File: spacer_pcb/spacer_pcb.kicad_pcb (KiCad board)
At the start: 2 copper layers, 10 x 39.3 mm, 3 parts, among them J1 Conn_01x15, J2 Conn_02x15_Odd_Even, J3 Conn_01x15

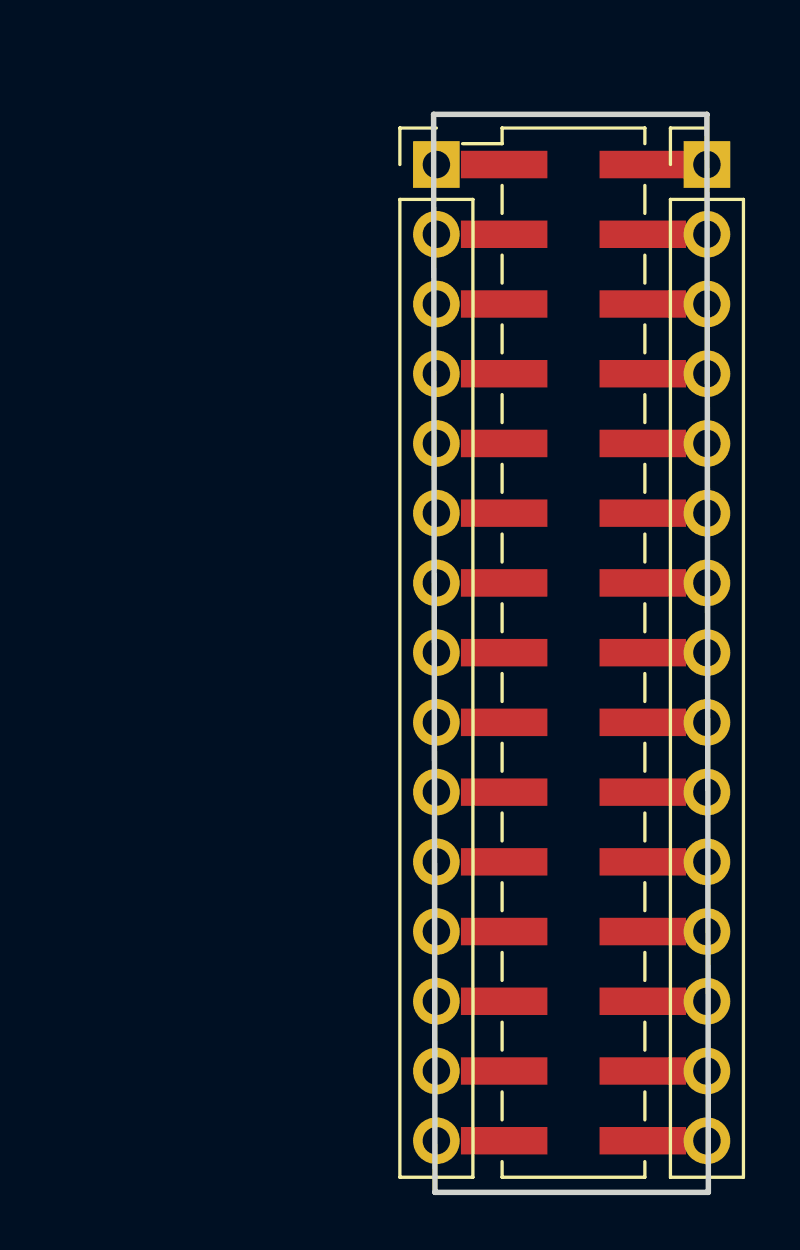
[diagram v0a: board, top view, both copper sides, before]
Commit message: Update connecting hole position between pcb and spacer pcb
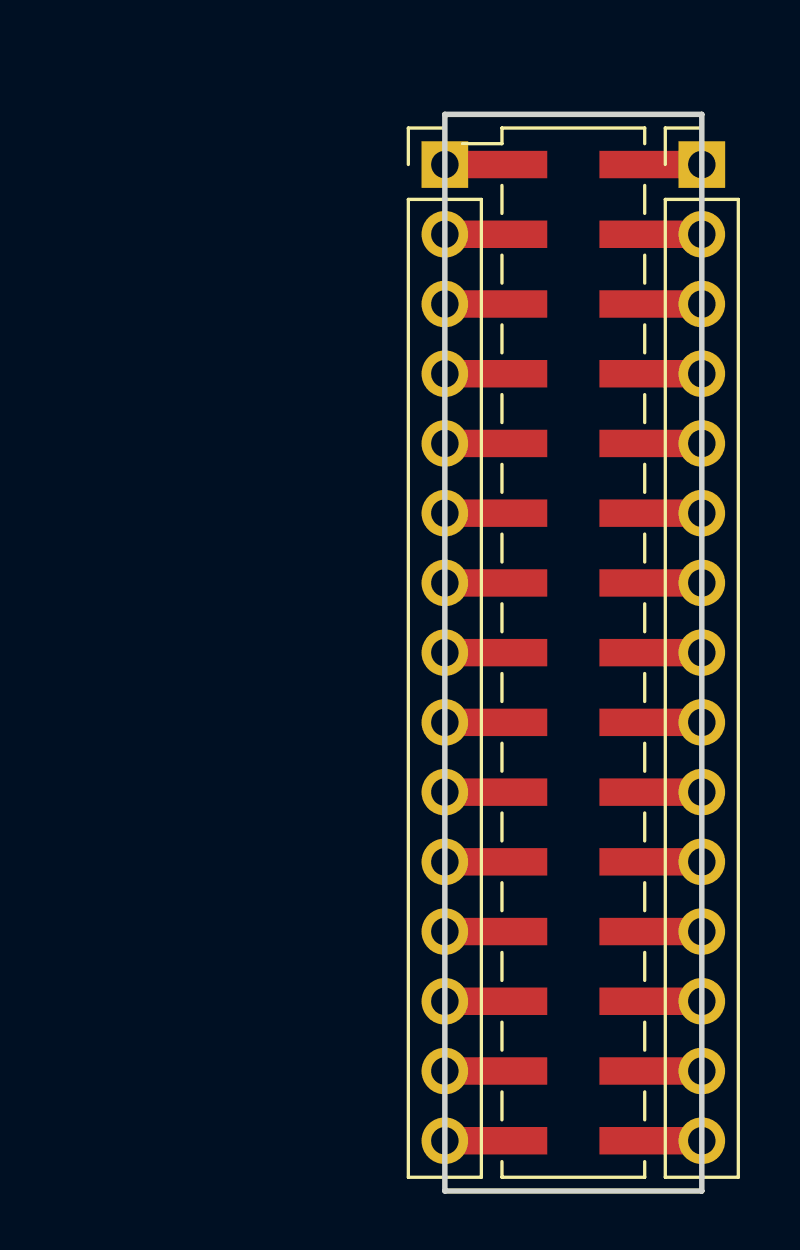
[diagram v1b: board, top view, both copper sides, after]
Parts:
- moved J1 0.31 mm to (131.2, 63.6)
- moved J3 0.19 mm to (140.6, 63.6)
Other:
- board size 10 x 39.3 mm -> 9.4 x 39.2 mm
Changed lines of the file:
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@@
   )
   (module Connector_PinHeader_2.54mm:PinHeader_1x15_P2.54mm_Vertical (layer F.Cu)
-    (at 130.9116 63.5508)
+    (at 131.22 63.5508)
     (descr "Through hole straight pin header, 1x15, 2.54mm pitch, single row")
     (tags "Through hole pin header THT 1x15 2.54mm single row")
@@
   )
   (module Connector_PinHeader_2.54mm:PinHeader_2x15_P2.54mm_Vertical_SMD (layer F.Cu)
-    (at 135.905 81.3308)
+    (at 135.9 81.3308)
     (descr "surface-mounted straight pin header, 2x15, 2.54mm pitch, double rows")
     (tags "Surface mounted pin header SMD 2x15 2.54mm double row")
@@
   )
   (module Connector_PinHeader_2.54mm:PinHeader_1x15_P2.54mm_Vertical (layer F.Cu)
-    (at 140.7668 63.5508)
+    (at 140.58 63.5508)
     (descr "Through hole straight pin header, 1x15, 2.54mm pitch, single row")
     (tags "Through hole pin header THT 1x15 2.54mm single row")
@@
     )
   )
-  (gr_line (start 140.7668 61.722) (end 130.81 61.722) (layer Edge.Cuts) (width 0.2))
-  (gr_line (start 140.8176 100.9904) (end 140.7668 61.722) (layer Edge.Cuts) (width 0.2))
-  (gr_line (start 130.8608 100.9904) (end 140.8176 100.9904) (layer Edge.Cuts) (width 0.2))
-  (gr_line (start 130.81 61.722) (end 130.8608 100.9904) (layer Edge.Cuts) (width 0.2))
+  (gr_line (start 140.58 61.722) (end 131.22 61.722) (layer Edge.Cuts) (width 0.2))
+  (gr_line (start 140.58 100.9396) (end 140.58 61.722) (layer Edge.Cuts) (width 0.2))
+  (gr_line (start 131.22 100.9396) (end 140.58 100.9396) (layer Edge.Cuts) (width 0.2))
+  (gr_line (start 131.22 61.722) (end 131.22 100.9396) (layer Edge.Cuts) (width 0.2))
 )

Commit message: Update revision and gerbers
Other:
- board text added: "spacer REV1.0 for M5StackSideBB REV1.1"
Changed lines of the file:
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@@
   (general
     (thickness 1.6)
-    (drawings 4)
+    (drawings 5)
     (tracks 0)
     (zones 0)
@@
       (outputformat 1)
       (mirror false)
-      (drillshape 1)
+      (drillshape 0)
       (scaleselection 1)
-      (outputdirectory ""))
+      (outputdirectory "gerbers"))
   )
   (net 0 "")
@@
     )
   )
+  (gr_text "spacer REV1.0 for M5StackSideBB REV1.1" (at 135.89 72.2884 270) (layer F.SilkS)
+    (effects (font (size 0.6 0.6) (thickness 0.15)))
+  )
   (gr_line (start 140.58 61.722) (end 131.22 61.722) (layer Edge.Cuts) (width 0.2))

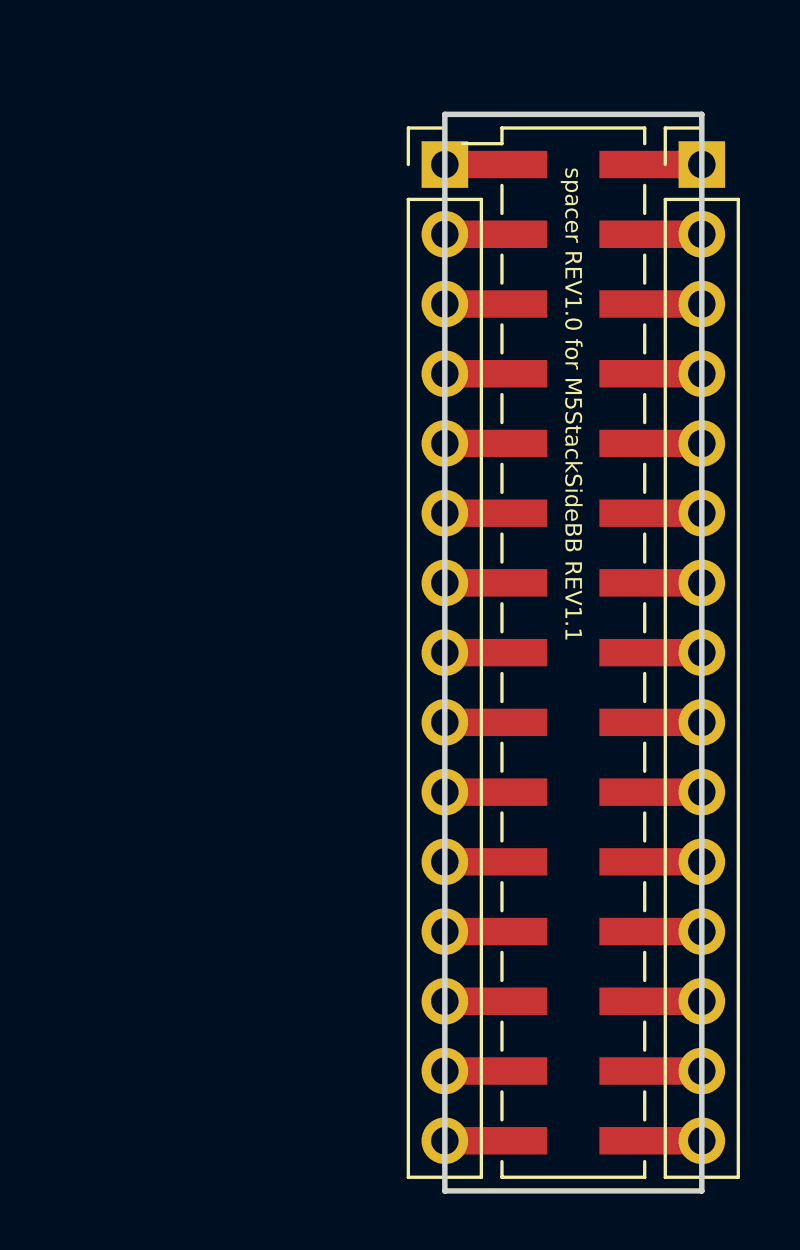
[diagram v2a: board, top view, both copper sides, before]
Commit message: Assign new footprint for spacer
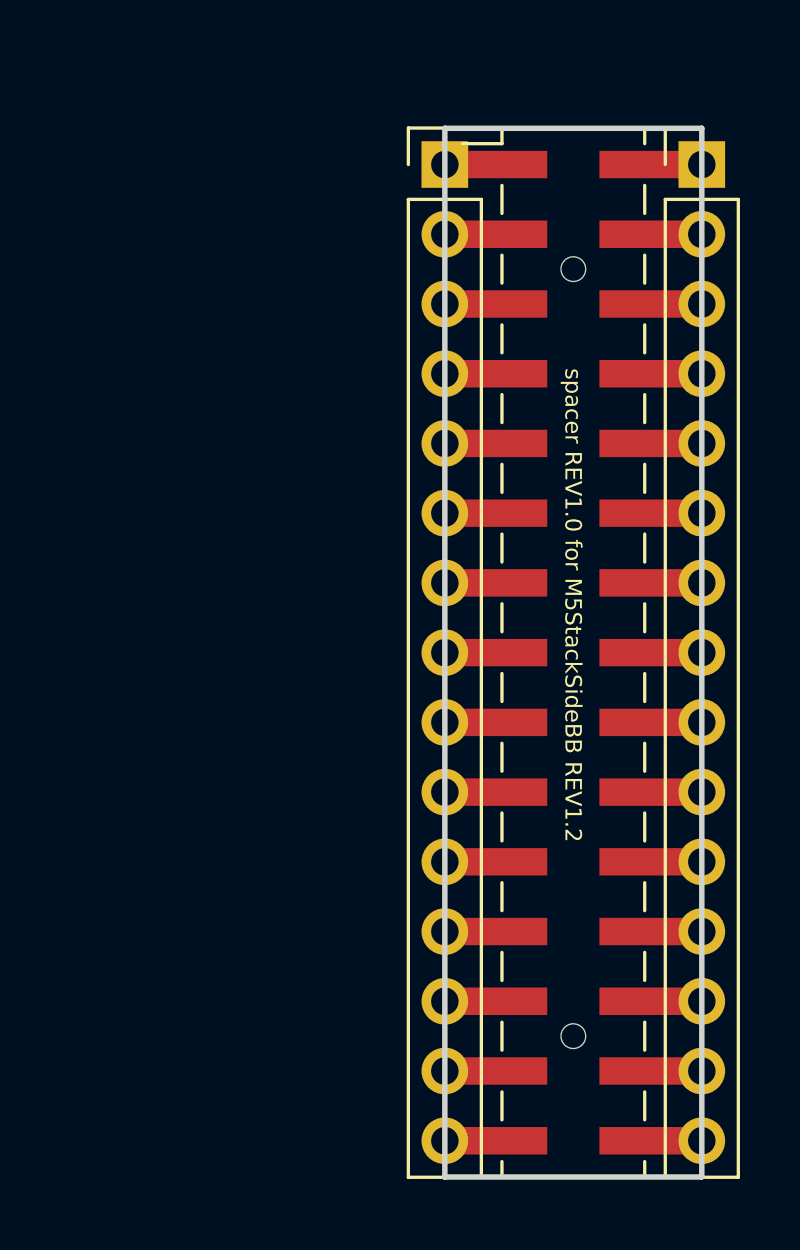
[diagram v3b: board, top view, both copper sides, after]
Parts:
- J2: footprint Connector_PinHeader_2.54mm:PinHeader_2x15_P2.54mm_Vertical_SMD -> footprints:PinHeader_2x15_P2.54mm_Vertical_SMD_for_M5Stack
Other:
- board size 9.4 x 39.2 mm -> 9.4 x 38.2 mm
- board text added: "spacer REV1.0 for M5StackSideBB REV1.2"
- board text removed: "spacer REV1.0 for M5StackSideBB REV1.1"
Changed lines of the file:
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@@
-(kicad_pcb (version 20171130) (host pcbnew 5.0.0-rc3-6a2723a~65~ubuntu17.10.1)
+(kicad_pcb (version 20171130) (host pcbnew 5.0.0-fee4fd1~65~ubuntu17.10.1)
   (general
     (thickness 1.6)
@@
     (add_net "Net-(J2-Pad8)")
   )
-  (module Connector_PinHeader_2.54mm:PinHeader_1x15_P2.54mm_Vertical (layer F.Cu)
-    (at 131.22 63.5508)
-    (descr "Through hole straight pin header, 1x15, 2.54mm pitch, single row")
-    (tags "Through hole pin header THT 1x15 2.54mm single row")
-    (fp_text reference J1 (at 0 -2.33) (layer F.SilkS) hide
-      (effects (font (size 1 1) (thickness 0.15)))
-    )
-    (fp_text value Conn_01x15 (at 0 37.89) (layer F.Fab)
-      (effects (font (size 1 1) (thickness 0.15)))
-    )
-    (fp_text user %R (at 0 17.78 90) (layer F.Fab)
-      (effects (font (size 1 1) (thickness 0.15)))
-    )
-    (fp_line (start 1.8 -1.8) (end -1.8 -1.8) (layer F.CrtYd) (width 0.05))
-    (fp_line (start 1.8 37.35) (end 1.8 -1.8) (layer F.CrtYd) (width 0.05))
-    (fp_line (start -1.8 37.35) (end 1.8 37.35) (layer F.CrtYd) (width 0.05))
-    (fp_line (start -1.8 -1.8) (end -1.8 37.35) (layer F.CrtYd) (width 0.05))
-    (fp_line (start -1.33 -1.33) (end 0 -1.33) (layer F.SilkS) (width 0.12))
-    (fp_line (start -1.33 0) (end -1.33 -1.33) (layer F.SilkS) (width 0.12))
-    (fp_line (start -1.33 1.27) (end 1.33 1.27) (layer F.SilkS) (width 0.12))
-    (fp_line (start 1.33 1.27) (end 1.33 36.89) (layer F.SilkS) (width 0.12))
-    (fp_line (start -1.33 1.27) (end -1.33 36.89) (layer F.SilkS) (width 0.12))
-    (fp_line (start -1.33 36.89) (end 1.33 36.89) (layer F.SilkS) (width 0.12))
-    (fp_line (start -1.27 -0.635) (end -0.635 -1.27) (layer F.Fab) (width 0.1))
-    (fp_line (start -1.27 36.83) (end -1.27 -0.635) (layer F.Fab) (width 0.1))
-    (fp_line (start 1.27 36.83) (end -1.27 36.83) (layer F.Fab) (width 0.1))
-    (fp_line (start 1.27 -1.27) (end 1.27 36.83) (layer F.Fab) (width 0.1))
-    (fp_line (start -0.635 -1.27) (end 1.27 -1.27) (layer F.Fab) (width 0.1))
-    (pad 15 thru_hole oval (at 0 35.56) (size 1.7 1.7) (drill 1) (layers *.Cu *.Mask)
-      (net 1 "Net-(J1-Pad15)"))
-    (pad 14 thru_hole oval (at 0 33.02) (size 1.7 1.7) (drill 1) (layers *.Cu *.Mask)
-      (net 2 "Net-(J1-Pad14)"))
-    (pad 13 thru_hole oval (at 0 30.48) (size 1.7 1.7) (drill 1) (layers *.Cu *.Mask)
-      (net 3 "Net-(J1-Pad13)"))
-    (pad 12 thru_hole oval (at 0 27.94) (size 1.7 1.7) (drill 1) (layers *.Cu *.Mask)
-      (net 4 "Net-(J1-Pad12)"))
-    (pad 11 thru_hole oval (at 0 25.4) (size 1.7 1.7) (drill 1) (layers *.Cu *.Mask)
-      (net 5 "Net-(J1-Pad11)"))
-    (pad 10 thru_hole oval (at 0 22.86) (size 1.7 1.7) (drill 1) (layers *.Cu *.Mask)
-      (net 6 "Net-(J1-Pad10)"))
-    (pad 9 thru_hole oval (at 0 20.32) (size 1.7 1.7) (drill 1) (layers *.Cu *.Mask)
-      (net 7 "Net-(J1-Pad9)"))
-    (pad 8 thru_hole oval (at 0 17.78) (size 1.7 1.7) (drill 1) (layers *.Cu *.Mask)
-      (net 8 "Net-(J1-Pad8)"))
-    (pad 7 thru_hole oval (at 0 15.24) (size 1.7 1.7) (drill 1) (layers *.Cu *.Mask)
-      (net 9 "Net-(J1-Pad7)"))
-    (pad 6 thru_hole oval (at 0 12.7) (size 1.7 1.7) (drill 1) (layers *.Cu *.Mask)
-      (net 10 "Net-(J1-Pad6)"))
-    (pad 5 thru_hole oval (at 0 10.16) (size 1.7 1.7) (drill 1) (layers *.Cu *.Mask)
-      (net 11 "Net-(J1-Pad5)"))
-    (pad 4 thru_hole oval (at 0 7.62) (size 1.7 1.7) (drill 1) (layers *.Cu *.Mask)
-      (net 12 "Net-(J1-Pad4)"))
-    (pad 3 thru_hole oval (at 0 5.08) (size 1.7 1.7) (drill 1) (layers *.Cu *.Mask)
-      (net 13 "Net-(J1-Pad3)"))
-    (pad 2 thru_hole oval (at 0 2.54) (size 1.7 1.7) (drill 1) (layers *.Cu *.Mask)
-      (net 14 "Net-(J1-Pad2)"))
-    (pad 1 thru_hole rect (at 0 0) (size 1.7 1.7) (drill 1) (layers *.Cu *.Mask)
-      (net 15 "Net-(J1-Pad1)"))
-    (model ${KISYS3DMOD}/Connector_PinHeader_2.54mm.3dshapes/PinHeader_1x15_P2.54mm_Vertical.wrl
-      (at (xyz 0 0 0))
-      (scale (xyz 1 1 1))
-      (rotate (xyz 0 0 0))
-    )
-  )
-  (module Connector_PinHeader_2.54mm:PinHeader_2x15_P2.54mm_Vertical_SMD (layer F.Cu)
+  (module footprints:PinHeader_2x15_P2.54mm_Vertical_SMD_for_M5Stack (layer F.Cu)
     (at 135.9 81.3308)
     (descr "surface-mounted straight pin header, 2x15, 2.54mm pitch, double rows")
@@
     (pad 30 smd rect (at 2.525 17.78) (size 3.15 1) (layers F.Cu F.Paste F.Mask)
       (net 30 "Net-(J2-Pad30)"))
+    (pad "" np_thru_hole circle (at 0 -13.97) (size 0.9 0.9) (drill 0.9) (layers *.Cu *.Mask))
+    (pad "" np_thru_hole circle (at 0 13.97) (size 0.9 0.9) (drill 0.9) (layers *.Cu *.Mask))
     (model ${KISYS3DMOD}/Connector_PinHeader_2.54mm.3dshapes/PinHeader_2x15_P2.54mm_Vertical_SMD.wrl
+      (at (xyz 0 0 0))
+      (scale (xyz 1 1 1))
+      (rotate (xyz 0 0 0))
+    )
+  )
+  (module Connector_PinHeader_2.54mm:PinHeader_1x15_P2.54mm_Vertical (layer F.Cu)
+    (at 131.22 63.5508)
+    (descr "Through hole straight pin header, 1x15, 2.54mm pitch, single row")
+    (tags "Through hole pin header THT 1x15 2.54mm single row")
+    (fp_text reference J1 (at 0 -2.33) (layer F.SilkS) hide
+      (effects (font (size 1 1) (thickness 0.15)))
+    )
+    (fp_text value Conn_01x15 (at 0 37.89) (layer F.Fab)
+      (effects (font (size 1 1) (thickness 0.15)))
+    )
+    (fp_text user %R (at 0 17.78 90) (layer F.Fab)
+      (effects (font (size 1 1) (thickness 0.15)))
+    )
+    (fp_line (start 1.8 -1.8) (end -1.8 -1.8) (layer F.CrtYd) (width 0.05))
+    (fp_line (start 1.8 37.35) (end 1.8 -1.8) (layer F.CrtYd) (width 0.05))
+    (fp_line (start -1.8 37.35) (end 1.8 37.35) (layer F.CrtYd) (width 0.05))
+    (fp_line (start -1.8 -1.8) (end -1.8 37.35) (layer F.CrtYd) (width 0.05))
+    (fp_line (start -1.33 -1.33) (end 0 -1.33) (layer F.SilkS) (width 0.12))
+    (fp_line (start -1.33 0) (end -1.33 -1.33) (layer F.SilkS) (width 0.12))
+    (fp_line (start -1.33 1.27) (end 1.33 1.27) (layer F.SilkS) (width 0.12))
+    (fp_line (start 1.33 1.27) (end 1.33 36.89) (layer F.SilkS) (width 0.12))
+    (fp_line (start -1.33 1.27) (end -1.33 36.89) (layer F.SilkS) (width 0.12))
+    (fp_line (start -1.33 36.89) (end 1.33 36.89) (layer F.SilkS) (width 0.12))
+    (fp_line (start -1.27 -0.635) (end -0.635 -1.27) (layer F.Fab) (width 0.1))
+    (fp_line (start -1.27 36.83) (end -1.27 -0.635) (layer F.Fab) (width 0.1))
+    (fp_line (start 1.27 36.83) (end -1.27 36.83) (layer F.Fab) (width 0.1))
+    (fp_line (start 1.27 -1.27) (end 1.27 36.83) (layer F.Fab) (width 0.1))
+    (fp_line (start -0.635 -1.27) (end 1.27 -1.27) (layer F.Fab) (width 0.1))
+    (pad 15 thru_hole oval (at 0 35.56) (size 1.7 1.7) (drill 1) (layers *.Cu *.Mask)
+      (net 1 "Net-(J1-Pad15)"))
+    (pad 14 thru_hole oval (at 0 33.02) (size 1.7 1.7) (drill 1) (layers *.Cu *.Mask)
+      (net 2 "Net-(J1-Pad14)"))
+    (pad 13 thru_hole oval (at 0 30.48) (size 1.7 1.7) (drill 1) (layers *.Cu *.Mask)
+      (net 3 "Net-(J1-Pad13)"))
+    (pad 12 thru_hole oval (at 0 27.94) (size 1.7 1.7) (drill 1) (layers *.Cu *.Mask)
+      (net 4 "Net-(J1-Pad12)"))
+    (pad 11 thru_hole oval (at 0 25.4) (size 1.7 1.7) (drill 1) (layers *.Cu *.Mask)
+      (net 5 "Net-(J1-Pad11)"))
+    (pad 10 thru_hole oval (at 0 22.86) (size 1.7 1.7) (drill 1) (layers *.Cu *.Mask)
+      (net 6 "Net-(J1-Pad10)"))
+    (pad 9 thru_hole oval (at 0 20.32) (size 1.7 1.7) (drill 1) (layers *.Cu *.Mask)
+      (net 7 "Net-(J1-Pad9)"))
+    (pad 8 thru_hole oval (at 0 17.78) (size 1.7 1.7) (drill 1) (layers *.Cu *.Mask)
+      (net 8 "Net-(J1-Pad8)"))
+    (pad 7 thru_hole oval (at 0 15.24) (size 1.7 1.7) (drill 1) (layers *.Cu *.Mask)
+      (net 9 "Net-(J1-Pad7)"))
+    (pad 6 thru_hole oval (at 0 12.7) (size 1.7 1.7) (drill 1) (layers *.Cu *.Mask)
+      (net 10 "Net-(J1-Pad6)"))
+    (pad 5 thru_hole oval (at 0 10.16) (size 1.7 1.7) (drill 1) (layers *.Cu *.Mask)
+      (net 11 "Net-(J1-Pad5)"))
+    (pad 4 thru_hole oval (at 0 7.62) (size 1.7 1.7) (drill 1) (layers *.Cu *.Mask)
+      (net 12 "Net-(J1-Pad4)"))
+    (pad 3 thru_hole oval (at 0 5.08) (size 1.7 1.7) (drill 1) (layers *.Cu *.Mask)
+      (net 13 "Net-(J1-Pad3)"))
+    (pad 2 thru_hole oval (at 0 2.54) (size 1.7 1.7) (drill 1) (layers *.Cu *.Mask)
+      (net 14 "Net-(J1-Pad2)"))
+    (pad 1 thru_hole rect (at 0 0) (size 1.7 1.7) (drill 1) (layers *.Cu *.Mask)
+      (net 15 "Net-(J1-Pad1)"))
+    (model ${KISYS3DMOD}/Connector_PinHeader_2.54mm.3dshapes/PinHeader_1x15_P2.54mm_Vertical.wrl
       (at (xyz 0 0 0))
       (scale (xyz 1 1 1))
@@
     )
   )
-  (gr_text "spacer REV1.0 for M5StackSideBB REV1.1" (at 135.89 72.2884 270) (layer F.SilkS)
+  (gr_text "spacer REV1.0 for M5StackSideBB REV1.2" (at 135.89 79.6036 270) (layer F.SilkS)
     (effects (font (size 0.6 0.6) (thickness 0.15)))
   )
-  (gr_line (start 140.58 61.722) (end 131.22 61.722) (layer Edge.Cuts) (width 0.2))
-  (gr_line (start 140.58 100.9396) (end 140.58 61.722) (layer Edge.Cuts) (width 0.2))
-  (gr_line (start 131.22 100.9396) (end 140.58 100.9396) (layer Edge.Cuts) (width 0.2))
-  (gr_line (start 131.22 61.722) (end 131.22 100.9396) (layer Edge.Cuts) (width 0.2))
+  (gr_line (start 140.5764 62.23) (end 131.2164 62.23) (layer Edge.Cuts) (width 0.2))
+  (gr_line (start 140.58 100.4316) (end 140.58 62.23) (layer Edge.Cuts) (width 0.2))
+  (gr_line (start 131.2036 100.4316) (end 140.5636 100.4316) (layer Edge.Cuts) (width 0.2))
+  (gr_line (start 131.22 62.23) (end 131.22 100.4316) (layer Edge.Cuts) (width 0.2))
 )
